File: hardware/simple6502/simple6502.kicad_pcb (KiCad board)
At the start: 2 copper layers, 100 x 100 mm, 37 parts, among them J1 ~{VP}, J2 CLK SEL, J3 RESET, J5 POWER 5V, J6 AUX 5VDC, SW1 RESET, SW2 POWER, T1 DS1813-10+, U1 W65C02SxP, U2 CY62256-70PC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

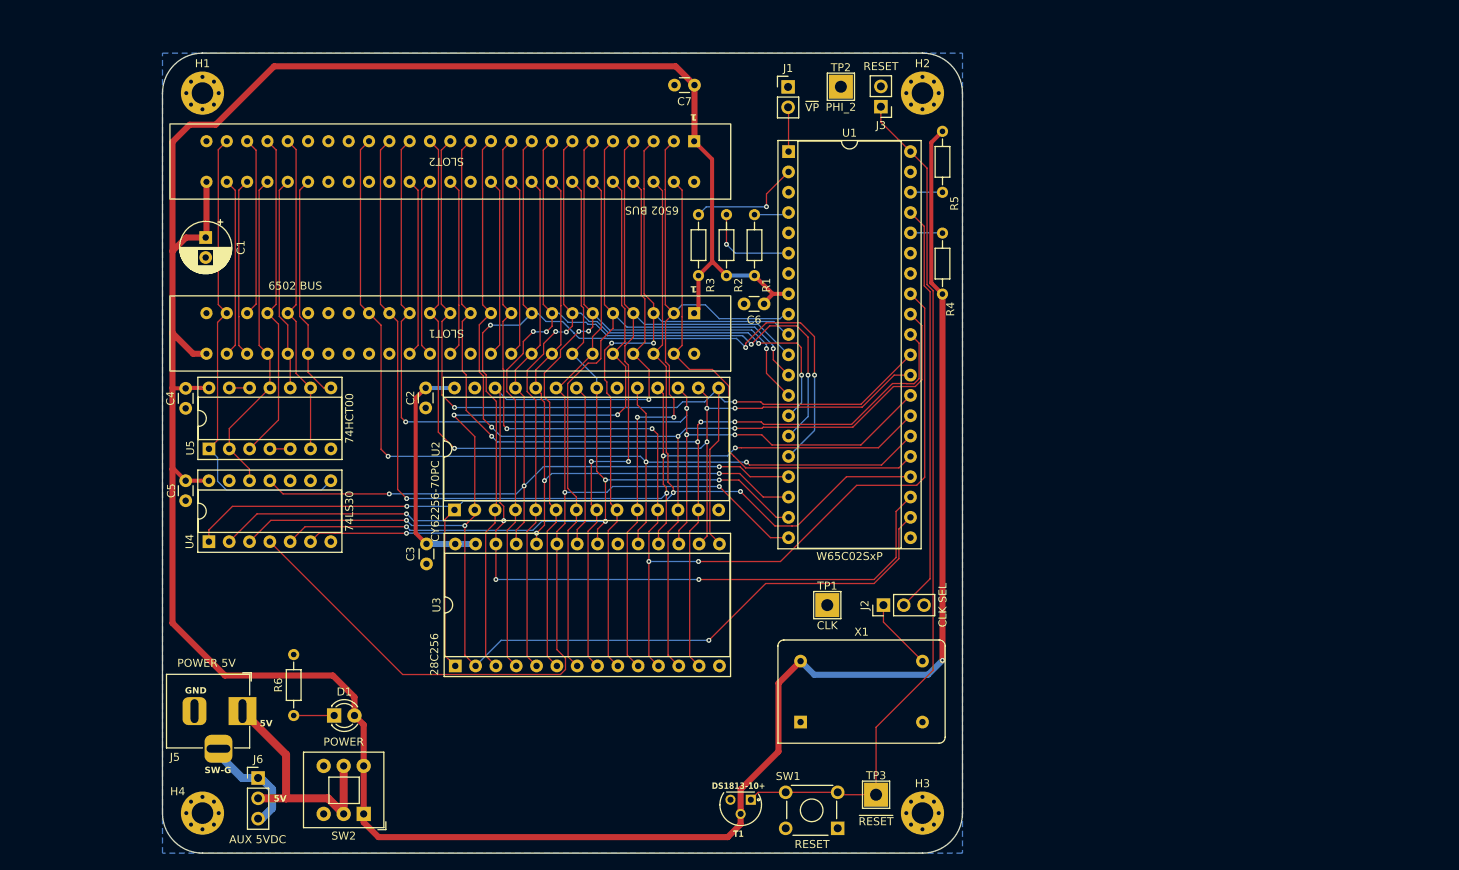
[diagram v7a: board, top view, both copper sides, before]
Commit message: PCB fully routed clean DRC
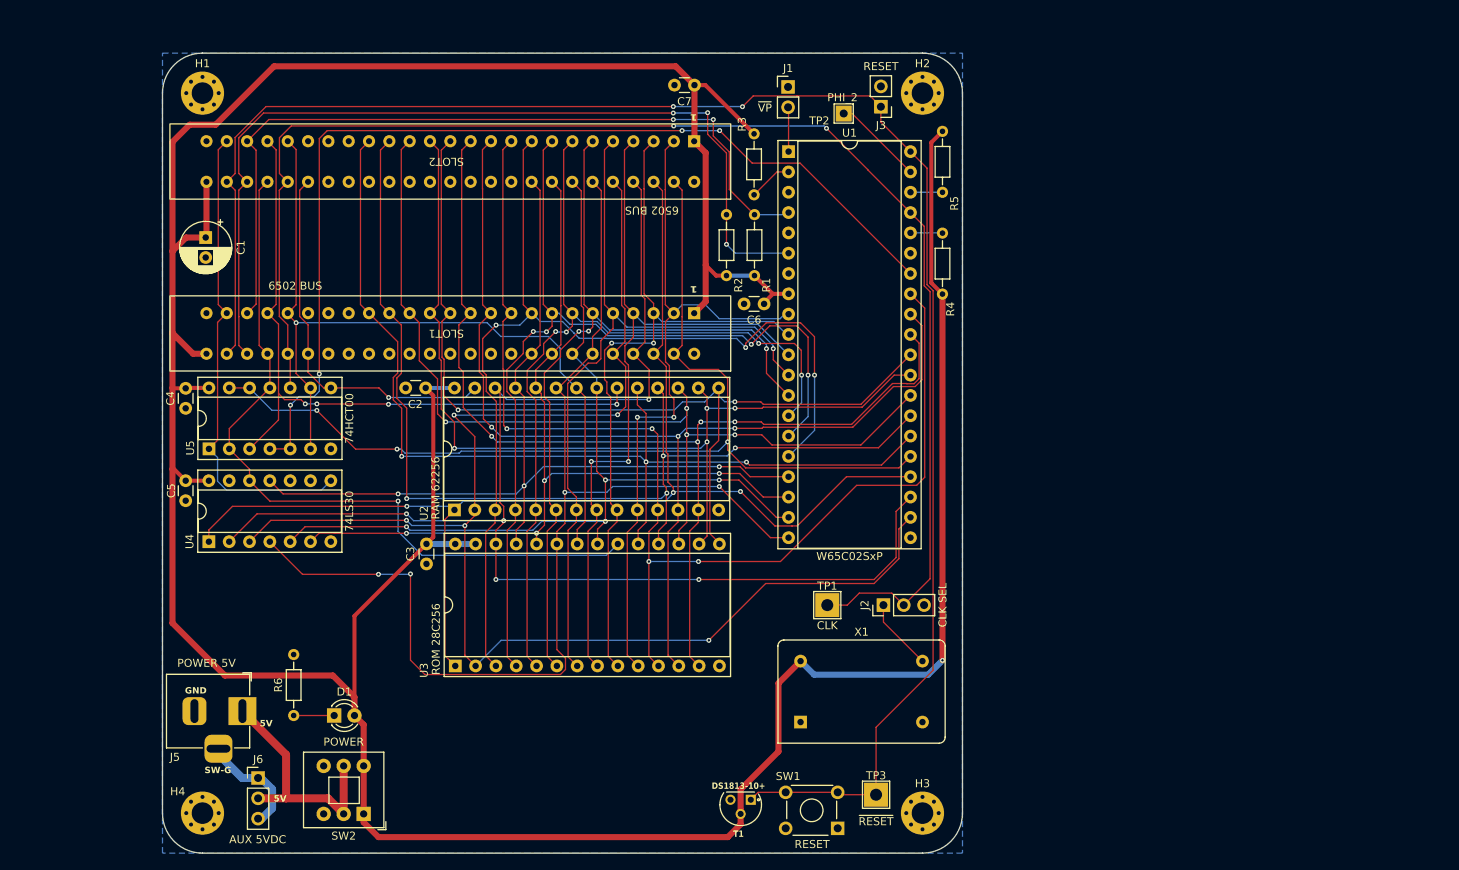
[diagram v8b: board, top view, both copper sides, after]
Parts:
- TP2: footprint TestPoint:TestPoint_THTPad_3.0x3.0mm_Drill1.5mm -> TestPoint:TestPoint_THTPad_2.0x2.0mm_Drill1.0mm
- U2: value CY62256-70PC -> RAM 62256
- U3: value 28C256 -> ROM 28C256
- moved R3 7.38 mm to (124.0, 67.7), turned to 90 degrees
- moved TP2 3.37 mm to (135.2, 57.5)
- turned C2 to 180 degrees
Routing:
- net R~{W}: track 2.54 -> 125.6 mm, vias 0 -> 4
- net CLK: track 78.2 -> 178.9 mm, vias 0 -> 2
- net ~{RESET}: track 130.2 -> 219.6 mm, vias 0 -> 2
- net ~{NMI}: track 34.3 -> 113.8 mm, vias 1 -> 3
- net ~{IRQ}: track 26.8 -> 100.2 mm, vias 0 -> 2
- net A15: track 65.7 -> 129.9 mm, vias 0 -> 3
- net VCC: track 432.1 -> 464.6 mm
- net ~{ROM_CS}: track 63.9 -> 94.2 mm, vias 0 -> 1
- net ~{RAM_CS}: track 63.8 -> 86.3 mm, vias 0 -> 4
- net ~{IO_CS}: track 82.2 -> 59.9 mm
- net ~{RD}: track 83.2 -> 101.0 mm, vias 0 -> 1
- net PHI_2: track 0.00 -> 11.4 mm
- net /RDY: track 14.4 -> 5.49 mm, vias 1 -> 0
- net A11: track 140.2 -> 146.6 mm, vias 2 -> 4
- net D5: track 124.4 -> 120.6 mm
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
